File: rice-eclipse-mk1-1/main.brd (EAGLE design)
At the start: 170.1 x 119.4 mm, 146 parts, among them IC1 LMV321LICTRT, IC10 MCP6N11R, IC11 MCP6N11R, IC12 MCP6N11R, IC2 LMV321LICTRT, IC3 LMV321LICTRT, IC4 LMV321LICTRT, IC5 MCP6N11R, IC6 LMV321LICTRT, IC7 LMV321LICTRT, IC8 LMV321LICTRT, IC9 LMV321LICTRT, U6 1101M2S3CQE2

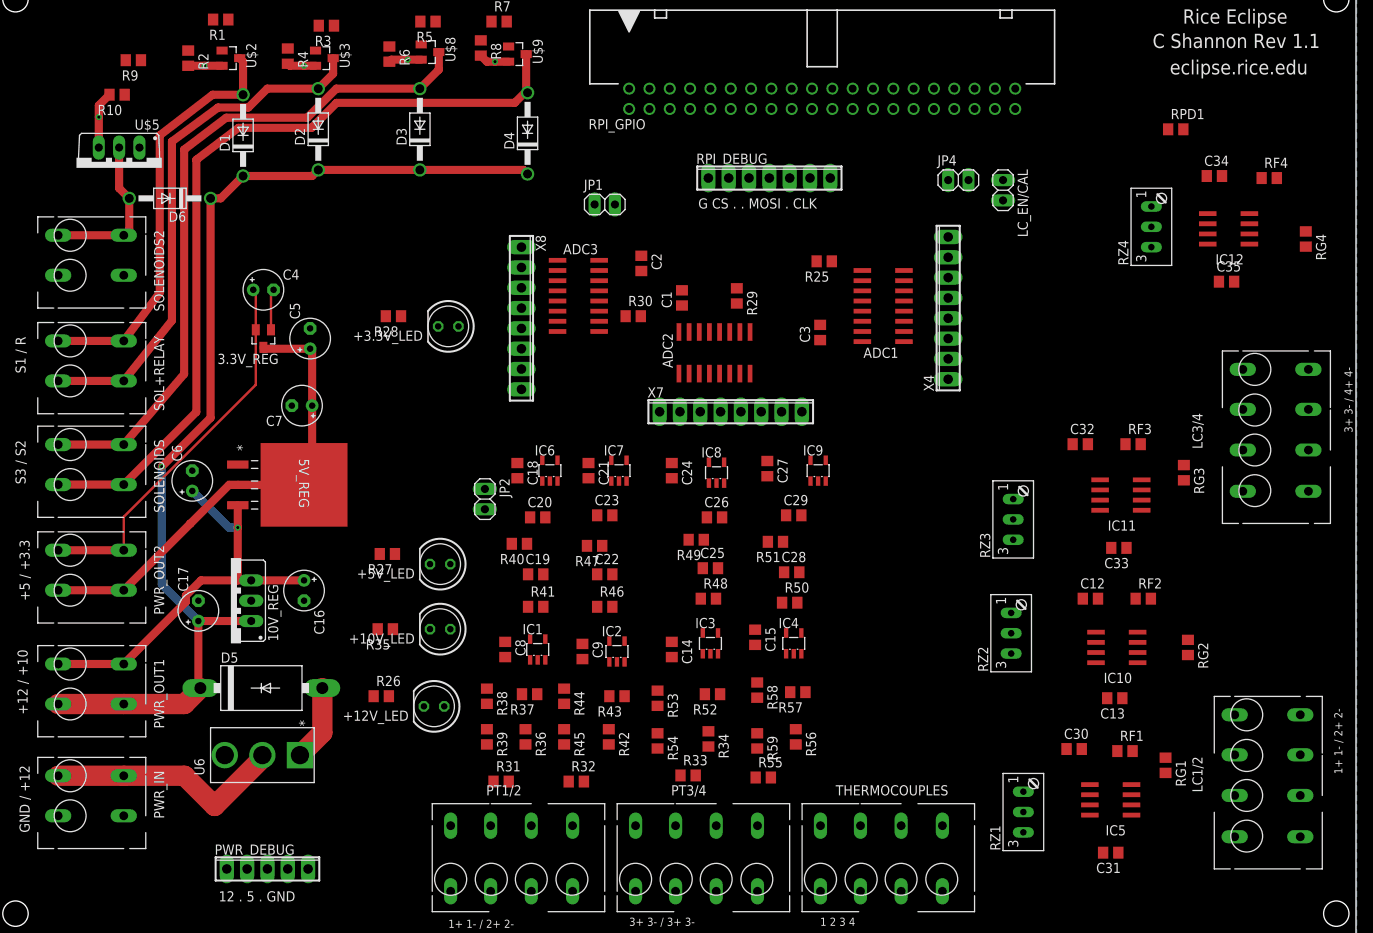
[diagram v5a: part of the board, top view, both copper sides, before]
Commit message: Added AA filter to lowpass output.
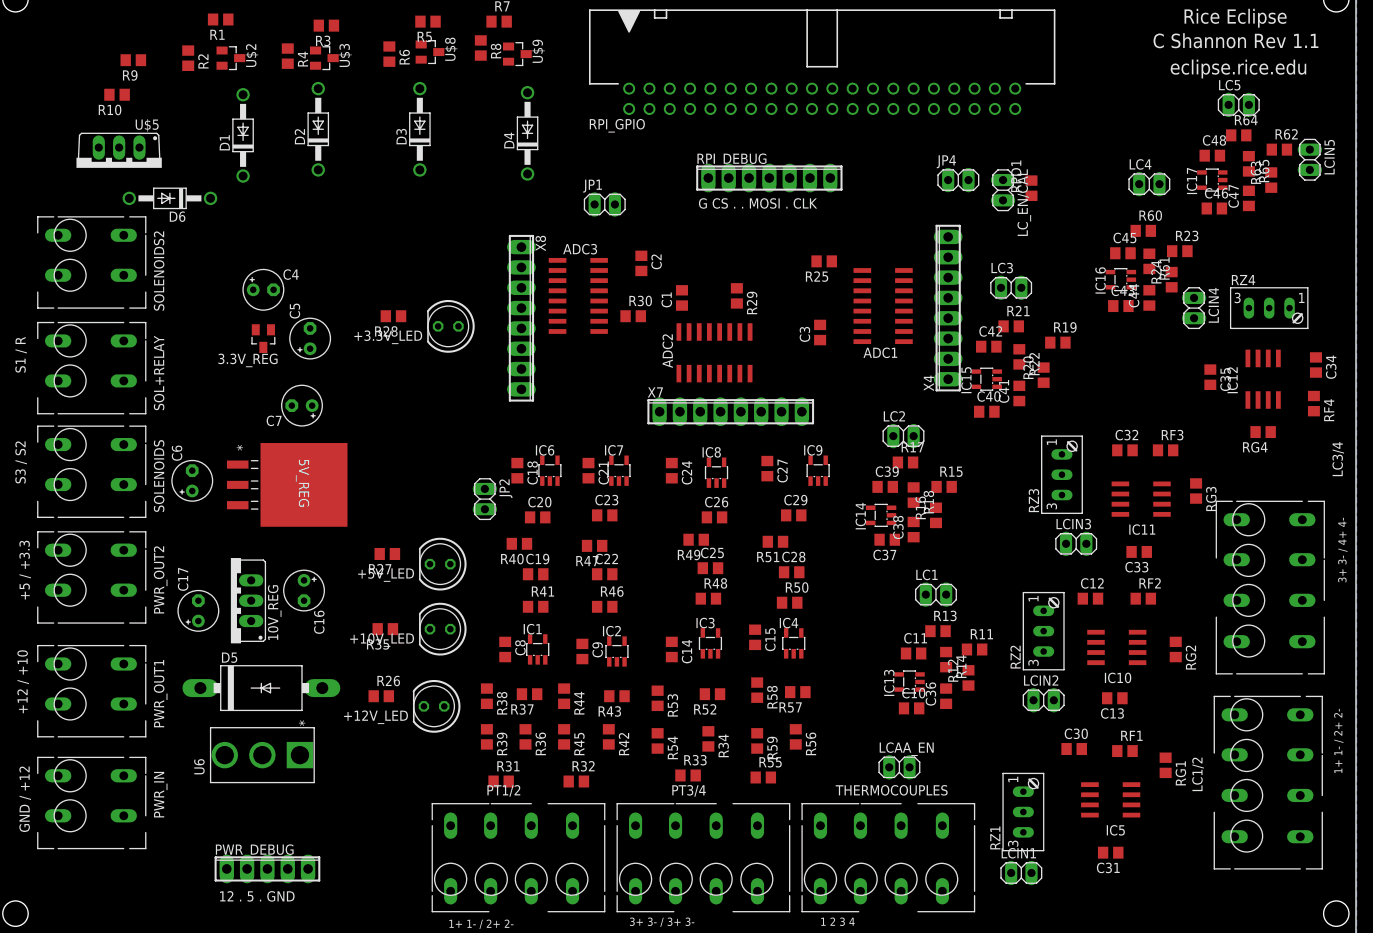
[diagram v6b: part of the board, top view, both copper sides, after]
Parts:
- added C10, C37, C40, C43, C46: 0.1UF, rcl:C0805
- added C11, C36, C38, C39, C41, C42, C44, C45: 1nF, rcl:C0805
- added C47, C48: ?, rcl:C0805
- added IC13, IC14, IC15, IC16, IC17: LMV321LICTRT, st-microelectronics-extra:SOT23-5
- added LC1, LC2, LC3, LC4, LC5, LCAA_EN, LCIN1, LCIN2, LCIN3, LCIN4, LCIN5: (no value), pinhead:1X02
- added R11, R15, R19, R23: 24.7K, rcl:R0805
- added R12, R16, R20, R24: 164K, rcl:R0805
- added R13, R17, R21, R60: 50.6K, rcl:R0805
- added R14, R18, R22, R61: 12.6K, rcl:R0805
- added R62, R63, R64, R65: ?, rcl:R0805
- moved RF4 28.7 mm to (164.8, 66.3), turned to 270 degrees
- moved C34 26.8 mm to (165.1, 71.1), turned to 270 degrees
- moved RG4 24.7 mm to (158.5, 62.7), turned to 180 degrees
- moved RPD1 19.5 mm to (129.5, 93.2), turned to 90 degrees
- moved IC12 19.3 mm to (158.5, 69.3), turned to 0 degrees
- moved LC3/4 18.8 mm to (155.2, 44.2)
- moved RZ4 17.7 mm to (159.3, 77.0), turned to 0 degrees
- moved C35 12.1 mm to (151.9, 69.6), turned to 270 degrees
- moved RZ3 8.27 mm to (134.6, 57.4)
- moved C32 5.64 mm to (141.2, 60.5)
- moved RF3 4.13 mm to (146.3, 60.5)
- moved RZ2 4.07 mm to (132.3, 37.8)
- moved RG3 2.75 mm to (150.1, 55.4)
- moved C33 2.59 mm to (143.0, 47.8)
- moved IC11 2.59 mm to (143.3, 54.4)
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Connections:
- new net +5V_LCAA: C10.1, C37.1, C40.1, C43.1, C46.1, IC13.5, IC14.5, IC15.5, IC16.5, IC17.5, LCAA_EN.2
- new net LC1_PREC: C31.2, IC5.6, LCIN1.2, RF1.1
- new net LC2_PREC: C13.2, IC10.6, LCIN2.2, RF2.1
- new net LC3_PREC: C33.2, IC11.6, LCIN3.2, RF3.1
- new net LC4_PREC: C35.2, IC12.6, LCIN4.2, RF4.1
- new net N$13: C11.1, R11.1, R12.2
- new net N$16: C36.1, IC13.1, R12.1
- new net N$17: C39.1, R15.1, R16.2
- new net N$18: C11.2, IC13.4, R13.1
- new net N$19: C38.1, IC14.1, R16.1
- new net N$20: C39.2, IC14.4, R17.1
- new net N$23: IC14.3, LC2.2, R17.2, R18.1
- new net N$24: C42.1, R19.1, R20.2
- new net N$38: C41.1, IC15.1, R20.1
- new net N$40: C42.2, IC15.4, R21.1
- new net N$44: IC15.3, LC3.2, R21.2, R22.1
- new net N$45: C45.1, R23.1, R24.2
- new net N$48: C44.1, IC16.1, R24.1
- new net N$49: C45.2, IC16.4, R60.1
- new net N$50: IC13.3, LC1.2, R13.2, R14.1
- new net N$51: IC16.3, LC4.2, R60.2, R61.1
- new net N$52: LCIN1.1, R11.2
- new net N$53: LCIN2.1, R15.2
- new net N$54: LCIN3.1, R19.2
- new net N$55: LCIN4.1, R23.2
- new net N$56: C48.1, R62.1, R63.2
- new net N$57: C47.1, IC17.1, R63.1
- new net N$58: C48.2, IC17.4, R64.1
- new net N$59: IC17.3, LC5.2, R64.2, R65.1
- new net N$60: LCIN5.1, R62.2
- net +5V: now also LCAA_EN.1
- net ADC1_A0: now also LC1.1; no longer C31.2, IC5.6, RF1.1
- net ADC1_A1: now also LC2.1; no longer C13.2, IC10.6, RF2.1
- net ADC1_A2: no longer C33.2, IC11.6, RF3.1
- net ADC1_A3: now also LC3.1; no longer C35.2, IC12.6, RF4.1
- net ADC1_A4: now also LC4.1
- net ADC1_A5: now also LC5.1
- net GND: now also C10.2, C36.2, C37.2, C38.2, C40.2, C41.2, C43.2, C44.2, C46.2, C47.2, IC13.2, IC14.2, IC15.2, IC16.2, IC17.2, R14.2, R18.2, R22.2, R61.2, R65.2
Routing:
- net +12V: track 132.3 -> 0.00 mm, vias 1 -> 0
- net SOLENOID_3_NEGATIVE: track 101.9 -> 0.00 mm
- net SOLENOID_2_NEGATIVE: track 85.7 -> 0.00 mm
- net SOLENOID_1_NEGATIVE: track 65.5 -> 0.00 mm
- net +5V: track 60.1 -> 0.00 mm
- net +10V: track 52.6 -> 0.00 mm, vias 1 -> 0
- net RELAY_NEGATIVE: track 52.3 -> 0.00 mm
- net +3V3: track 47.7 -> 0.00 mm
- net +12V_DEBUG: track 29.9 -> 0.00 mm
- net GND: track 28.0 -> 0.00 mm, vias 5 -> 0
- net SOLENOID_4_NEGATIVE: track 20.0 -> 0.00 mm
- net N$4: track 9.54 -> 0.00 mm

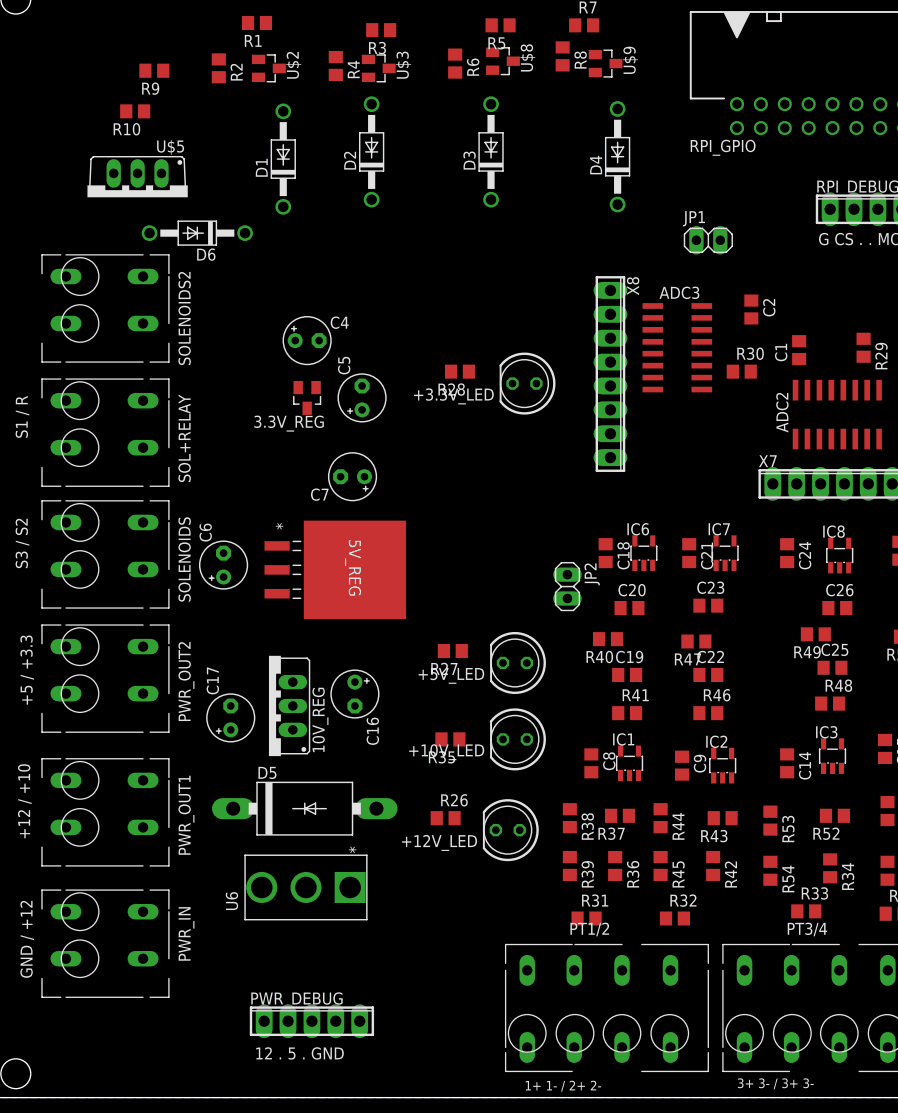
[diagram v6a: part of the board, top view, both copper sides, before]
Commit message: Updated board route a bit. Rest is autorouted.
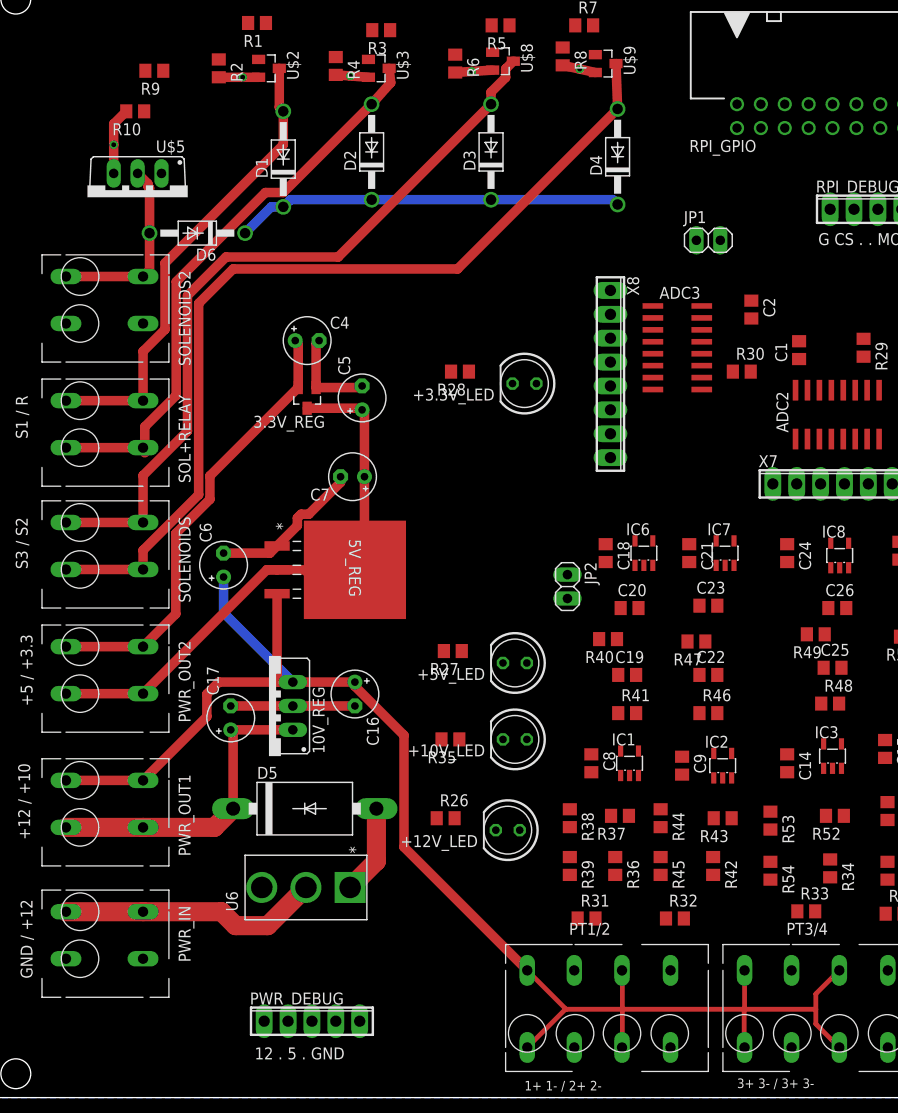
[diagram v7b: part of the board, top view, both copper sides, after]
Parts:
- R27: value 113 -> 140
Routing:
- net +10V: track 0.00 -> 164.8 mm
- net SOLENOID_3_NEGATIVE: track 0.00 -> 96.9 mm
- net SOLENOID_2_NEGATIVE: track 0.00 -> 80.6 mm
- net +12V: track 0.00 -> 75.0 mm
- net +5V: track 0.00 -> 64.6 mm
- net GND: track 0.00 -> 62.4 mm, vias 0 -> 5
- net SOLENOID_1_NEGATIVE: track 0.00 -> 61.2 mm
- net RELAY_NEGATIVE: track 0.00 -> 49.9 mm
- net +3V3: track 0.00 -> 47.7 mm
- net +12V_DEBUG: track 0.00 -> 27.8 mm
- net SOLENOID_4_NEGATIVE: track 0.00 -> 20.0 mm
- net N$4: track 0.00 -> 9.54 mm

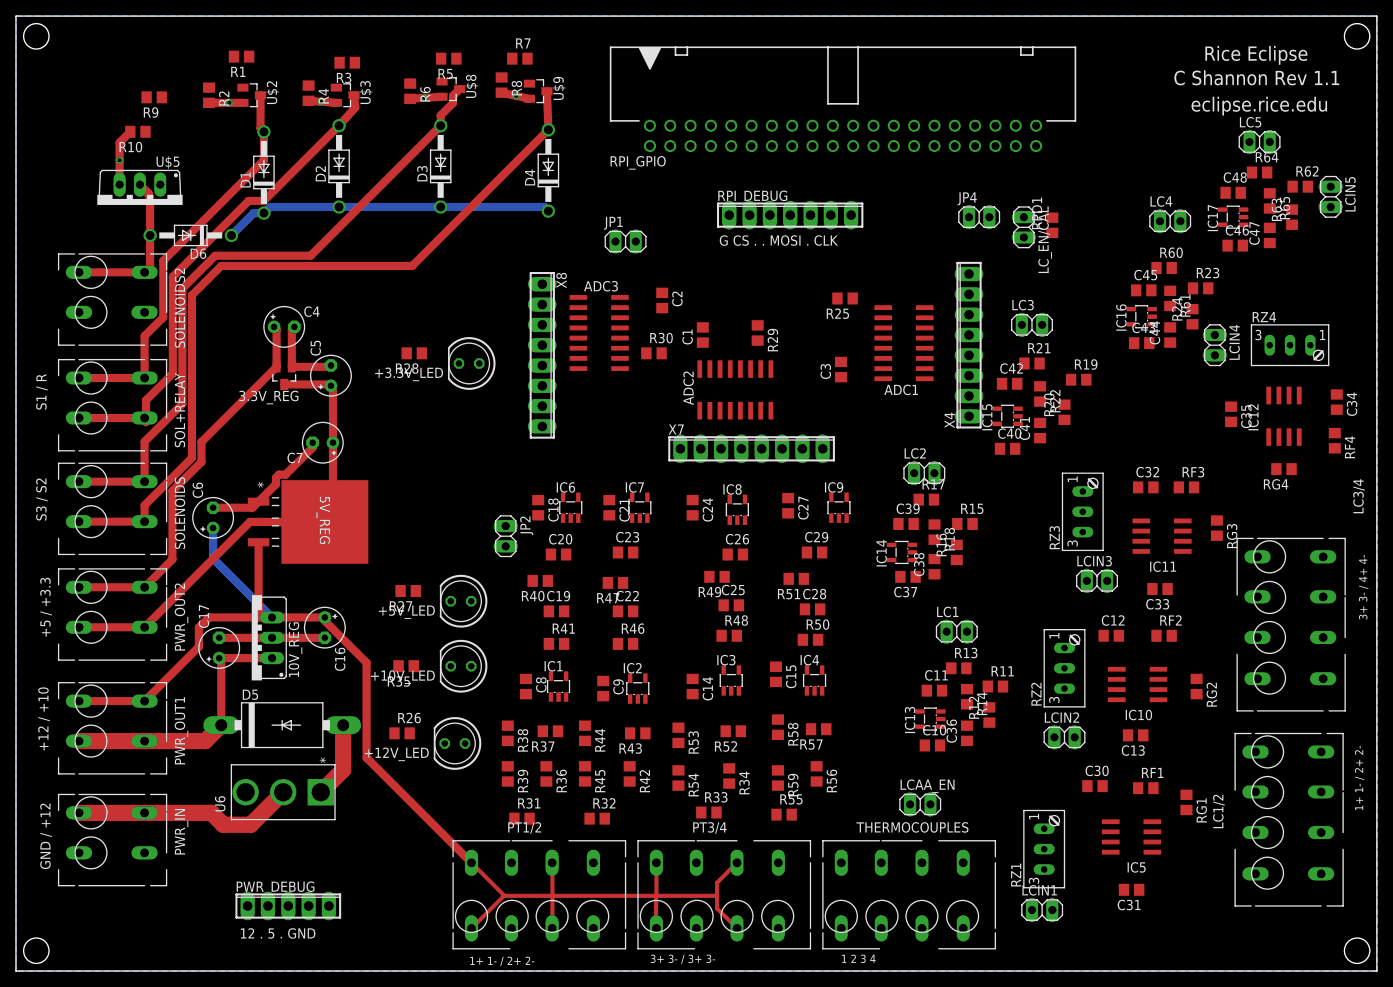
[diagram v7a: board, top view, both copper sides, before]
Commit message: Added final routing for version 1.1.
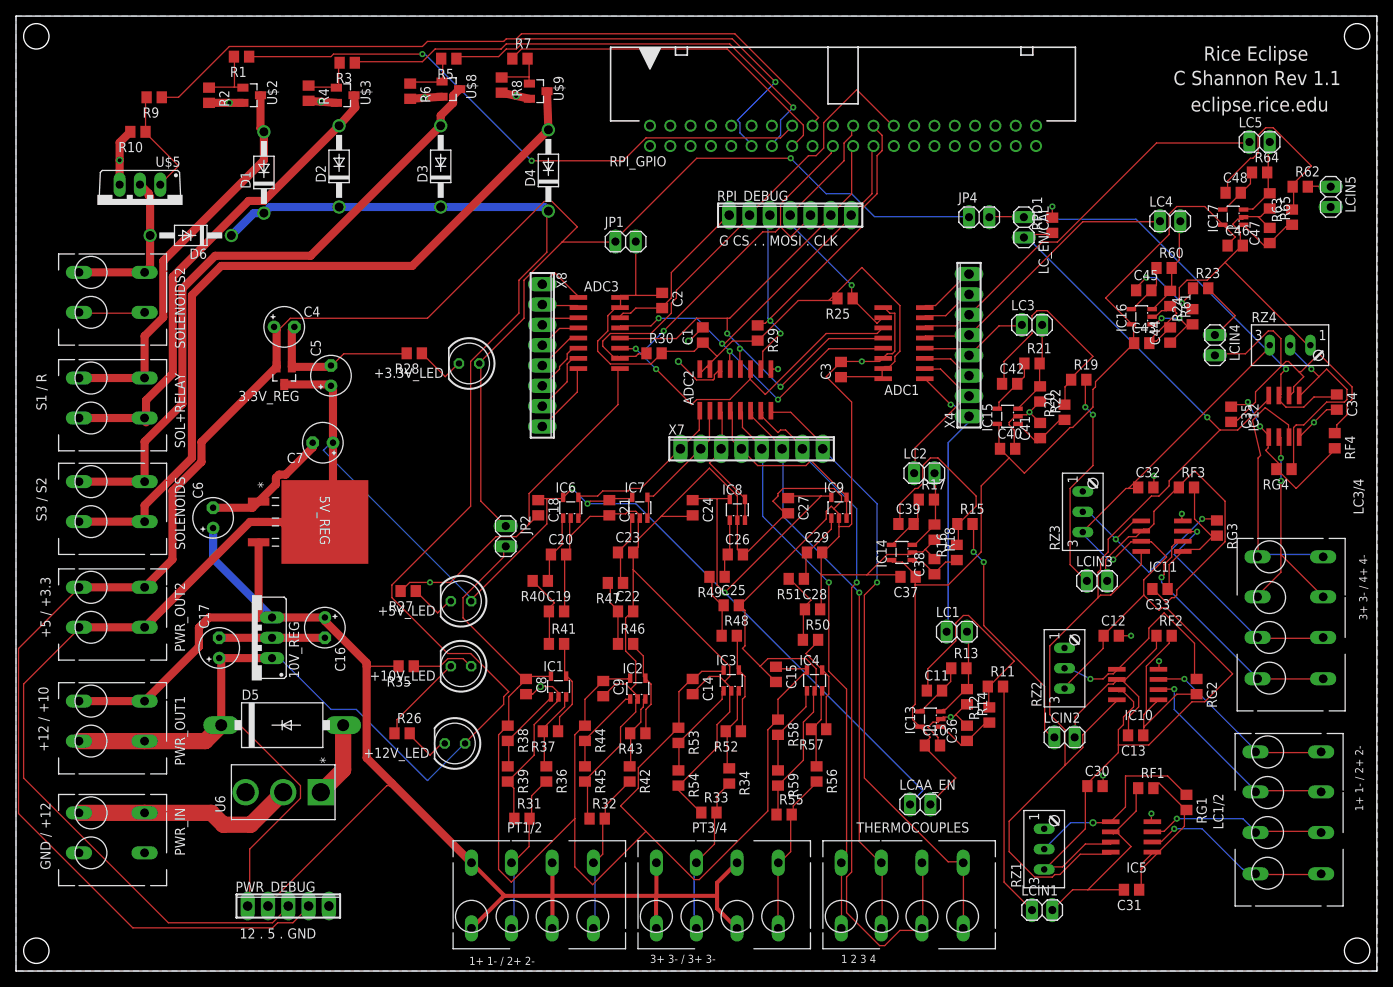
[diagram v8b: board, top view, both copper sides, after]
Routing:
- net GND: track 62.4 -> 570.9 mm, vias 5 -> 21
- net +3V3: track 47.7 -> 270.6 mm, vias 0 -> 1
- net +5V: track 64.6 -> 285.5 mm, vias 0 -> 3
- net +3V3_LC: track 0.00 -> 202.6 mm, vias 0 -> 2
- net +3V3_PT: track 0.00 -> 178.9 mm
- net +12V: track 75.0 -> 223.7 mm
- net CAL: track 0.00 -> 147.4 mm, vias 0 -> 1
- net +5V_LCAA: track 0.00 -> 122.6 mm
- net CTRL_SOLENOID_4: track 0.00 -> 91.3 mm
- net ADC2_A6: track 0.00 -> 89.7 mm, vias 0 -> 1
- net +3V3_ADC: track 0.00 -> 88.0 mm
- net MOSI: track 0.00 -> 85.0 mm, vias 0 -> 3
- net ADC2_A7: track 0.00 -> 78.6 mm, vias 0 -> 1
- net IGNITION_RELAY: track 0.00 -> 75.4 mm, vias 0 -> 2
- net SCLK: track 0.00 -> 75.4 mm, vias 0 -> 4
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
